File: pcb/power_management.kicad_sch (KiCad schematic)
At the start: 36 parts, among them J3 USB C, J4 2059-302/998-403, Q2 AO3400A, Q3 AO3401A, Q4 AO3401A, SW4 POWER, U4 BQ25619, U5 AP6683, U7 AMS1117-3.3

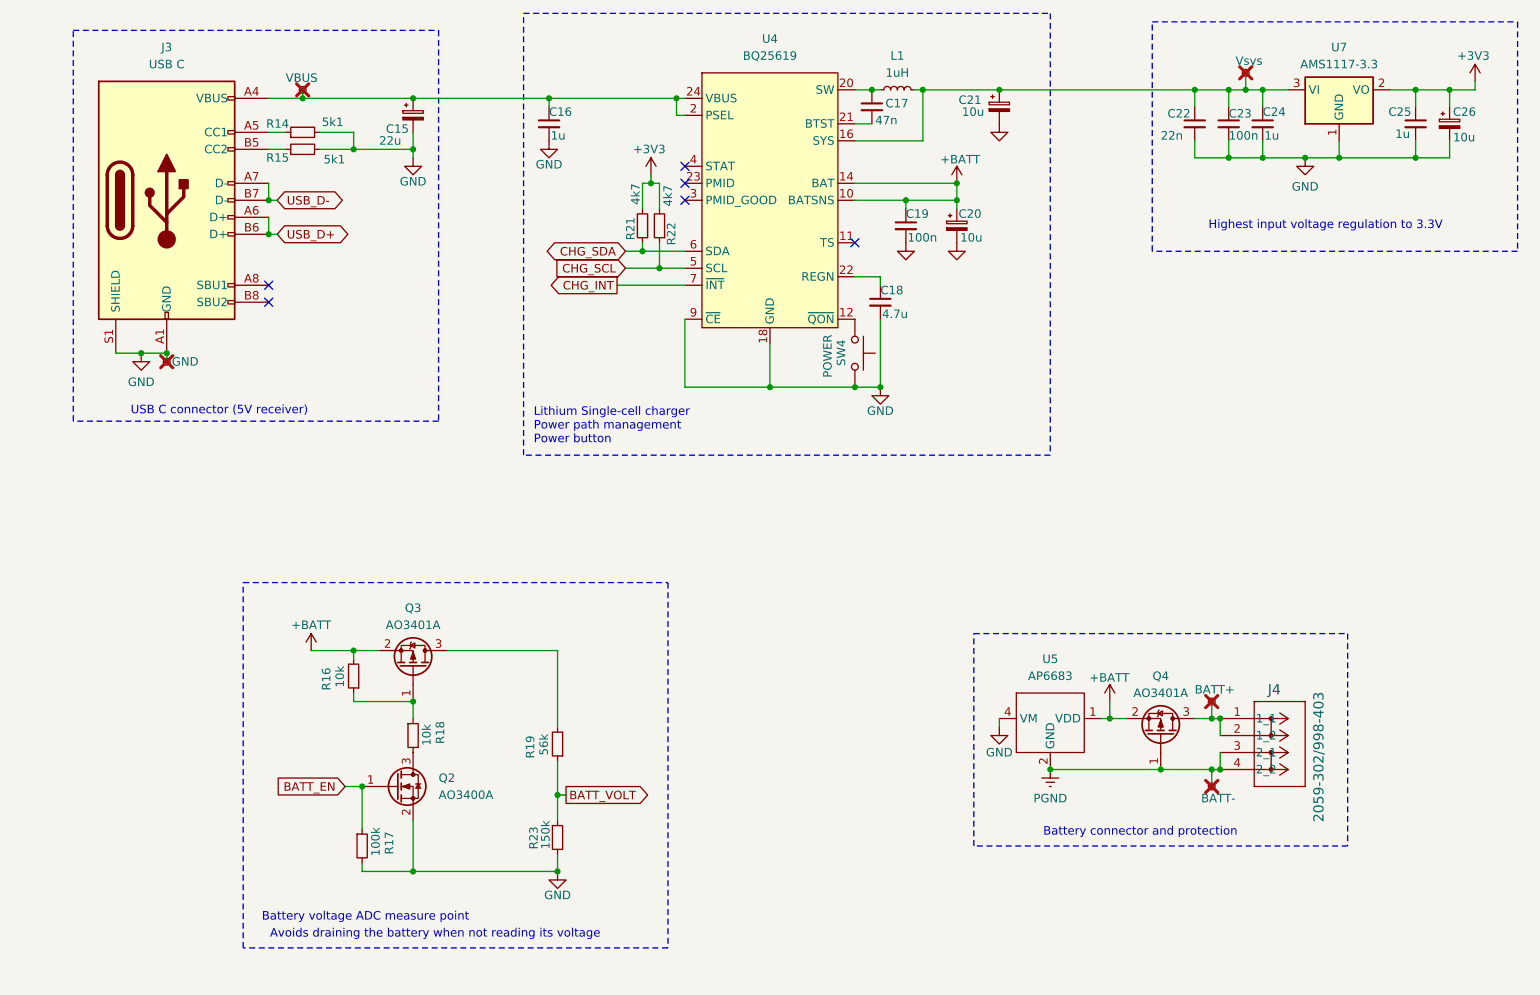
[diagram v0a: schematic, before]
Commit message: refactor: fallback to rev 0.3 and update files (#98)
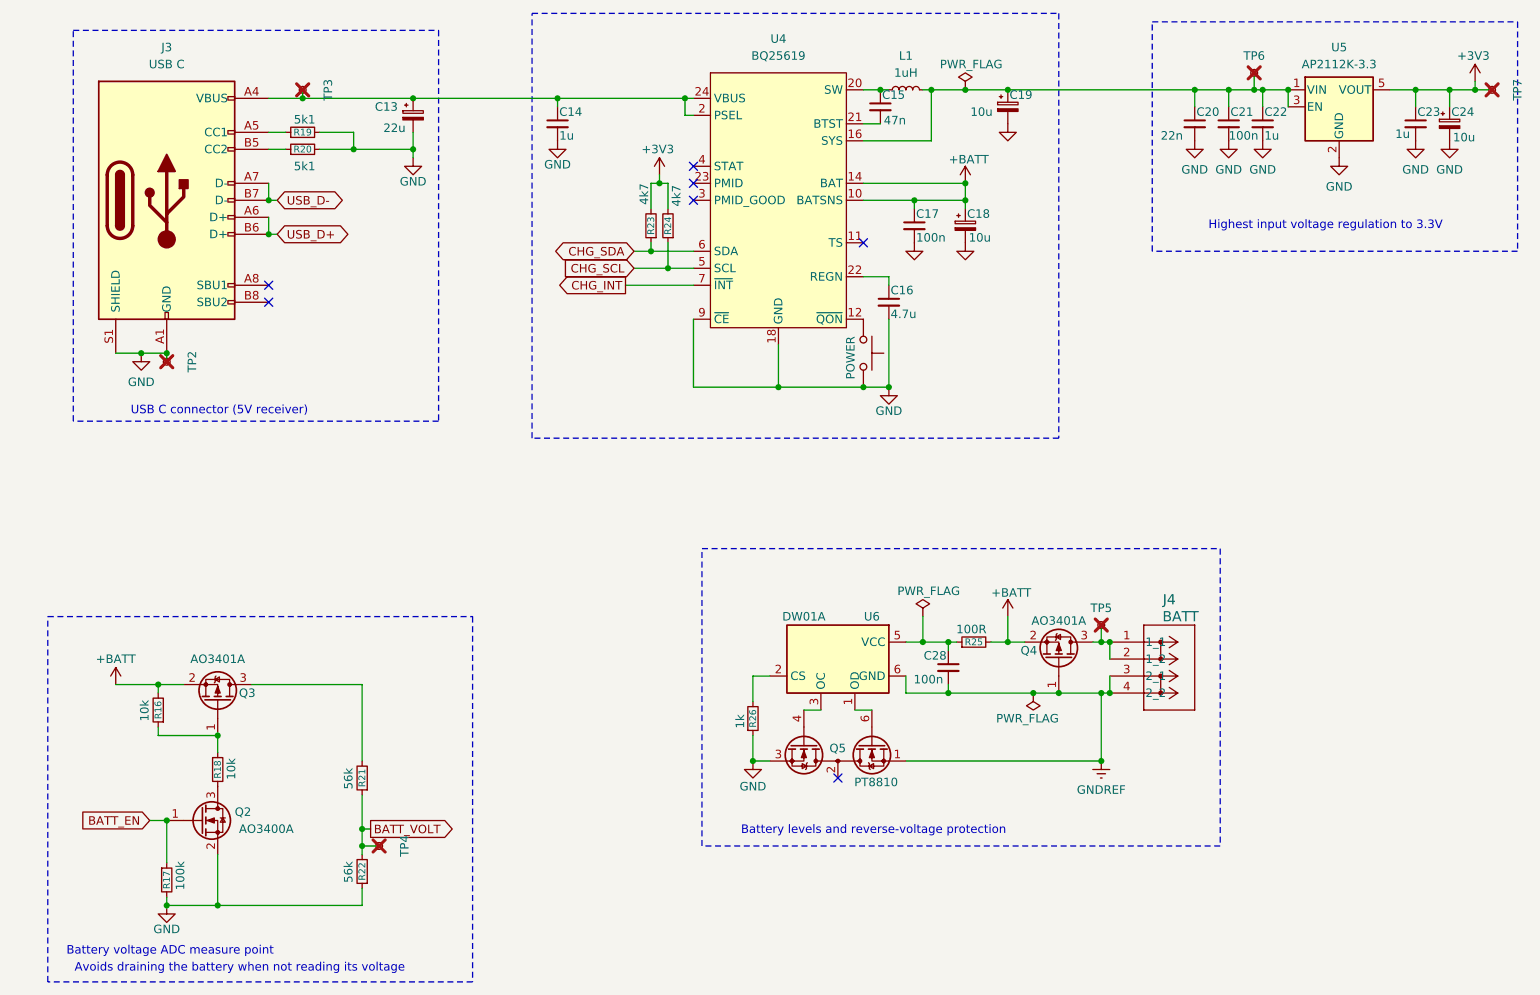
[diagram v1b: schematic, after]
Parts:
- removed C17: 47n, Capacitor_SMD:C_0603_1608Metric, symbol Device:C_Small
- removed C18: 4.7u, Capacitor_SMD:C_0805_2012Metric, symbol Device:C_Small
- removed R21: 4k7, leany_footprints:R_0402_1005Metric, symbol Device:R_Small
- removed TP6: BATT-, leany_footprints:TestPoint_Pad_1.0x1.0mm, symbol Connector:TestPoint_Small
- removed U5: AP6683, Package_DFN_QFN:UDFN-4-1EP_1x1mm_P0.65mm_EP0.48x0.48mm, symbol leany-symbols:AP6683
- removed U7: AMS1117-3.3, Package_TO_SOT_SMD:SOT-223-3_TabPin2, symbol Regulator_Linear:AMS1117-3.3
- added C14: 1u, leany_footprints:C_0402_1005Metric, symbol Device:C_Small
- added C15: 47n, Capacitor_SMD:C_0603_1608Metric, symbol Device:C_Small
- added C28: 100n, leany_footprints:C_0402_1005Metric, symbol Device:C_Small
- added Q5: PT8810, Package_TO_SOT_SMD:SOT-23-6, symbol leany-symbols:PT8810
- added R24: 4k7, leany_footprints:R_0402_1005Metric, symbol Device:R_Small
- added R25: 100R, leany_footprints:R_0402_1005Metric, symbol Device:R_Small
- added R26: 1k, leany_footprints:R_0402_1005Metric, symbol Device:R_Small
- added TP4: BATT, leany_footprints:TestPoint_Pad_1.0x1.0mm, symbol Connector:TestPoint_Small
- added TP7: 3.3V, leany_footprints:TestPoint_Pad_1.0x1.0mm, symbol Connector:TestPoint_Small
- added U5: AP2112K-3.3, Package_TO_SOT_SMD:SOT-23-5, symbol Regulator_Linear:AP2112K-3.3
- added U6: DW01A, Package_TO_SOT_SMD:SOT-23-6, symbol Battery_Management:DW01A
- C16: value 1u -> 4.7u; footprint leany_footprints:C_0402_1005Metric -> Capacitor_SMD:C_0805_2012Metric; LCSC C52923 -> C1779
- J3: LCSC C2765186 -> C136423
- J4: value 2059-302/998-403 -> BATT
- R22: value 4k7 -> 56k; footprint leany_footprints:R_0402_1005Metric -> Resistor_SMD:R_0603_1608Metric; LCSC C25900 -> C23206
- R23: value 150k -> 4k7; footprint Resistor_SMD:R_0603_1608Metric -> leany_footprints:R_0402_1005Metric; LCSC C22807 -> C25900
- TP5: value BATT+ -> +BATT
- TP6: renamed from TP7; value Vsys -> Vin
- renumbered C15 to C13, C19 to C17, C20 to C18, C21 to C19, C22 to C20, C23 to C21, C24 to C22, C25 to C23, C26 to C24, R14 to R19, R15 to R20, R19 to R21, SW4 to SW5
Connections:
- net +3V3: now also R23.2, R24.2, TP7.1, U5.5 (VOUT); no longer R22.2
- net +BATT: now also R25.2
- net BATT_VOLT: now also R22.2, TP4.1; no longer R23.1
- net CHG_SCL: now also R24.1; no longer R22.1
- net CHG_SDA: now also R23.1
- net GND: now also R22.1, C14.2, Q5.3 (S2), R26.1, U5.2 (GND); no longer R23.2
- net at L1.1, U4.19 (SW), U4.20 (SW): now also C15.1
- net SYS: now reaches C19.1, C20.1, C21.1, C22.1, L1.2, TP6.1, U4.15 (SYS), U4.16 (SYS)
- net SYS: now also U5.1 (VIN), U5.3 (EN)
- net at U4.21 (BTST): now also C15.2
- net at U4.22 (REGN): now also C16.1
- net at C13.1, J3.A4 (VBUS), J3.A9 (VBUS)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: now also C14.1; no longer C16.1
- net PGND renamed GNDREF
- net GNDREF: now also C28.2, Q5.1 (D1), U6.6 (GND)
- new net: C28.1, R25.1, U6.5 (VCC)
- new net: Q5.6 (G1), U6.1 (OD)
- new net: R26.2, U6.2 (CS)
- new net: Q5.4 (G2), U6.3 (OC)
- new net: Q5.2 (S1/D2), Q5.5 (S1/D2)
- no-connect marks 6 -> 7
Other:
- note added: "Battery levels and reverse-voltage protection"
- note removed: "Battery connector and protection"
- note removed: "Lithium Single-cell charger Power path management Power button"
- moved on the sheet: C17, C18, C19, L1, Q2, Q3, R16, R17, R18, R21

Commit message: fix: remove test points from BOM  and CPL (#98)
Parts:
- TP2, TP3, TP5, TP6, TP7: now left out of the parts list
- TP4: value BATT -> VBATT; now left out of the parts list
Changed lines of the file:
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@@
 		(dnp no)
 		(property "Reference" "C21"
-			(at 213.614 40.132 0)
+			(at 213.36 40.005 0)
 			(show_name no)
 			(do_not_autoplace no)
@@
 		)
 		(property "Value" "100n"
-			(at 213.36 43.688 0)
+			(at 213.36 43.815 0)
 			(show_name no)
 			(do_not_autoplace no)
@@
 		(body_style 1)
 		(exclude_from_sim no)
-		(in_bom yes)
+		(in_bom no)
 		(on_board yes)
-		(in_pos_files yes)
+		(in_pos_files no)
 		(dnp yes)
 		(property "Reference" "TP3"
-			(at 78.74 36.83 0)
+			(at 74.93 34.925 90)
+			(hide yes)
 			(show_name no)
 			(do_not_autoplace no)
@@
 		)
 		(property "Value" "VBUS"
-			(at 73.6601 35.56 0)
-			(hide yes)
+			(at 72.39 34.925 90)
 			(show_name no)
 			(do_not_autoplace no)
@@
 			)
 		)
-		(property "LCSC" ""
-			(at 74.93 36.83 0)
-			(hide yes)
-			(show_name no)
-			(do_not_autoplace no)
-			(effects
-				(font
-					(size 1.27 1.27)
-				)
-			)
-		)
 		(pin "1"
 		)
@@
 		(body_style 1)
 		(exclude_from_sim no)
-		(in_bom yes)
+		(in_bom no)
 		(on_board yes)
-		(in_pos_files yes)
+		(in_pos_files no)
 		(dnp yes)
 		(property "Reference" "TP5"
 			(at 194.31 114.3 0)
+			(hide yes)
 			(show_name no)
 			(do_not_autoplace no)
@@
 		)
 		(property "Value" "+BATT"
-			(at 195.58 118.1099 0)
-			(hide yes)
+			(at 193.04 114.935 0)
 			(show_name no)
 			(do_not_autoplace no)
@@
 			)
 		)
-		(property "LCSC" ""
-			(at 194.31 116.84 0)
-			(hide yes)
-			(show_name no)
-			(do_not_autoplace no)
-			(effects
-				(font
-					(size 1.27 1.27)
-				)
-			)
-		)
 		(pin "1"
 		)
@@
 		(body_style 1)
 		(exclude_from_sim no)
-		(in_bom yes)
+		(in_bom no)
 		(on_board yes)
-		(in_pos_files yes)
+		(in_pos_files no)
 		(dnp yes)
 		(property "Reference" "TP4"
 			(at 90.17 149.86 0)
+			(hide yes)
 			(show_name no)
 			(do_not_autoplace no)
@@
 			)
 		)
-		(property "Value" "BATT"
-			(at 85.0901 151.13 0)
-			(hide yes)
+		(property "Value" "VBATT"
+			(at 87.63 149.86 90)
 			(show_name no)
 			(do_not_autoplace no)
@@
 			)
 		)
-		(property "LCSC" ""
-			(at 86.36 149.86 0)
-			(hide yes)
-			(show_name no)
-			(do_not_autoplace no)
-			(effects
-				(font
-					(size 1.27 1.27)
-				)
-			)
-		)
 		(pin "1"
 		)
@@
 		)
 		(property "Value" "1u"
-			(at 218.694 43.688 0)
+			(at 220.345 41.91 0)
 			(show_name no)
 			(do_not_autoplace no)
@@
 		(dnp no)
 		(property "Reference" "C20"
-			(at 208.534 40.132 0)
+			(at 203.835 40.005 0)
 			(show_name no)
 			(do_not_autoplace no)
@@
 		)
 		(property "Value" "22n"
-			(at 203.2 43.688 0)
+			(at 203.835 43.815 0)
 			(show_name no)
 			(do_not_autoplace no)
@@
 		(body_style 1)
 		(exclude_from_sim no)
-		(in_bom yes)
+		(in_bom no)
 		(on_board yes)
-		(in_pos_files yes)
+		(in_pos_files no)
 		(dnp yes)
 		(property "Reference" "TP2"
 			(at 58.42 77.47 0)
+			(hide yes)
 			(show_name no)
 			(do_not_autoplace no)
@@
 		)
 		(property "Value" "GND"
-			(at 53.3401 76.2 0)
-			(hide yes)
+			(at 55.245 77.47 90)
 			(show_name no)
 			(do_not_autoplace no)
@@
 			)
 		)
-		(property "LCSC" ""
-			(at 54.61 77.47 0)
-			(hide yes)
-			(show_name no)
-			(do_not_autoplace no)
-			(effects
-				(font
-					(size 1.27 1.27)
-				)
-			)
-		)
 		(pin "1"
 		)
@@
 		(body_style 1)
 		(exclude_from_sim no)
-		(in_bom yes)
+		(in_bom no)
 		(on_board yes)
-		(in_pos_files yes)
+		(in_pos_files no)
 		(dnp yes)
 		(property "Reference" "TP6"
 			(at 217.17 31.75 0)
+			(hide yes)
 			(show_name no)
 			(do_not_autoplace no)
@@
 		)
 		(property "Value" "Vin"
-			(at 218.44 35.5599 0)
-			(hide yes)
+			(at 215.9 32.385 0)
 			(show_name no)
 			(do_not_autoplace no)
@@
 			)
 		)
-		(property "LCSC" ""
-			(at 217.17 34.29 0)
-			(hide yes)
-			(show_name no)
-			(do_not_autoplace no)
-			(effects
-				(font
-					(size 1.27 1.27)
-				)
-			)
-		)
 		(pin "1"
 		)
@@
 		(body_style 1)
 		(exclude_from_sim no)
-		(in_bom yes)
+		(in_bom no)
 		(on_board yes)
-		(in_pos_files yes)
+		(in_pos_files no)
 		(dnp yes)
 		(property "Reference" "TP7"
 			(at 256.54 36.83 0)
+			(hide yes)
 			(show_name no)
 			(do_not_autoplace no)
@@
 		)
 		(property "Value" "3.3V"
-			(at 251.4601 38.1 0)
-			(hide yes)
+			(at 254.635 34.925 0)
 			(show_name no)
 			(do_not_autoplace no)
@@
 			(at 252.73 36.83 0)
 			(hide yes)
-			(show_name no)
-			(do_not_autoplace no)
-			(effects
-				(font
-					(size 1.27 1.27)
-				)
-			)
-		)
-		(property "LCSC" ""
-			(at 252.73 36.83 0)
-			(hide yes)
